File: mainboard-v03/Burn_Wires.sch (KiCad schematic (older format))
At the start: 41 parts, among them Q2 2N5088, Q3 2N5088, Q4 IRLML2803, Q5 IRLML2803, Q6 IRLML2803, Q7 IRLML2803, Q8 IRLML2803, U16 PE014006, U17 PE014006, U18 NDS8434, U19 NDS8434, U20 NDS8434, U21 NDS8434, U22 NDS8434

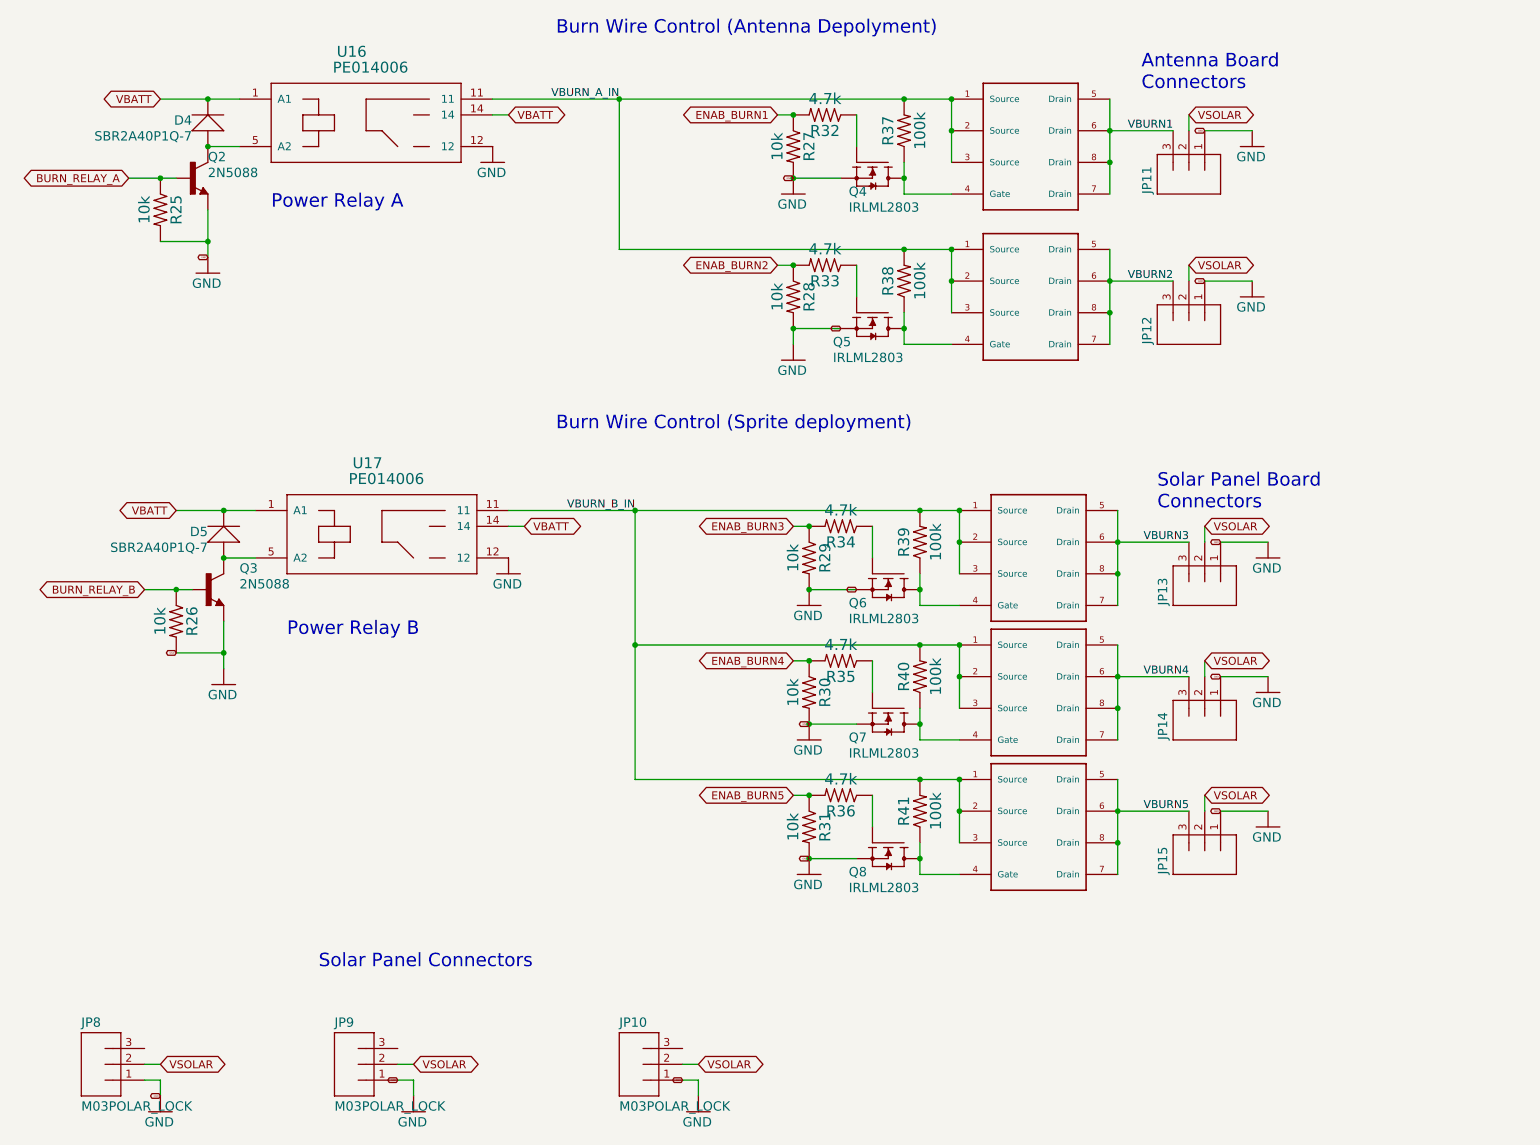
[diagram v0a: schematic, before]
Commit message: cleaning up schematic scheets
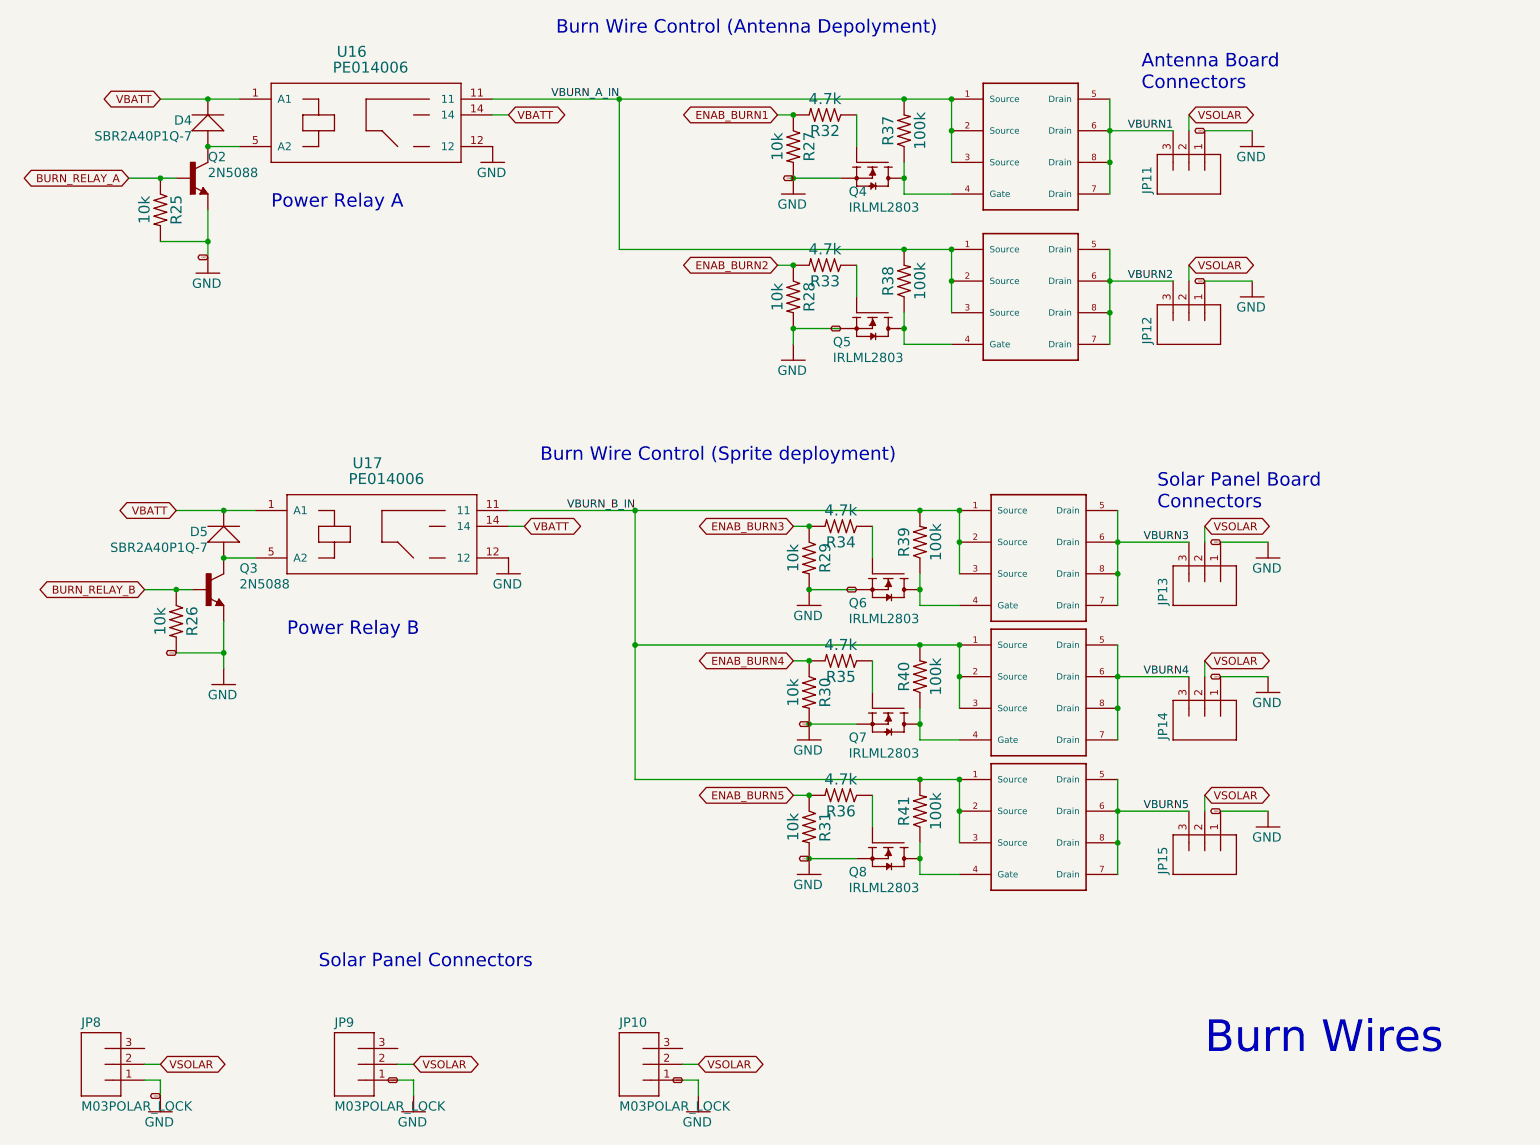
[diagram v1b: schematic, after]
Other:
- note added: "Burn Wires"
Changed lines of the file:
@@
 $Descr User 11693 8548
 encoding utf-8
-Sheet 6 6
+Sheet 2 6
 Title "PyCubed Mainboard"
 Date ""
-Rev "v02"
+Rev "v03"
 Comp "Stanford University"
 Comment1 "rexlab.stanford.edu"
@@
 Text Notes 4500 800  0    85   ~ 0
 Burn Wire Control (Antenna Depolyment)
-Text Notes 4500 3300 0    85   ~ 0
+Text Notes 4400 3500 0    85   ~ 0
 Burn Wire Control (Sprite deployment)
 Text Notes 2800 4600 0    85   ~ 0
@@
 Wire Wire Line
 	5000 3800 5000 4650
+Text Notes 8600 7250 0    200  ~ 0
+Burn Wires
 $EndSCHEMATC

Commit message: mainboardv3 clean up
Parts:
- removed D5: SBR2A40P1Q-7, kmb-test:PWRDI-123, symbol mainboard:DFLS130L
- removed Q3: 2N5088, kmb-test:SOT23, symbol mainboard:BC846
- removed Q6, Q7, Q8: IRLML2803, kmb-test:SOT-23, symbol mainboard:IRLML2803TRPBF
- removed R26, R29, R30, R31: 10k, Resistor_SMD:R_0603_1608Metric, symbol mainboard:RESISTOR0603
- removed R34, R35, R36: 4.7k, Resistor_SMD:R_0603_1608Metric, symbol mainboard:RESISTOR0603
- removed R39, R40, R41: 100k, Resistor_SMD:R_0603_1608Metric, symbol mainboard:RESISTOR0603
- removed U17: PE014006, kmb-test:RELAY5-PE_CO, symbol mainboard:PE014005
- removed U20, U21, U22: NDS8434, custom-footprints:NDS8434, symbol symbols:NDS8434
- D4: value SBR2A40P1Q-7 -> MBR120LSF; footprint kmb-test:PWRDI-123 -> mainboard:PWRDI-123
- JP10, JP11, JP12, JP13, JP14, JP15, JP8, JP9: footprint kmb-test:MOLEX-1X3_LOCK -> mainboard:MOLEX-1X3_LOCK
- Q2: footprint kmb-test:SOT23 -> mainboard:SOT23; Flight (none) -> 2N5088; Proto (none) -> S8050
- Q4: footprint kmb-test:SOT-23 -> mainboard:SOT-23; Flight (none) -> IRLML2803; Proto (none) -> 2302
- Q5: footprint kmb-test:SOT-23 -> mainboard:SOT-23
- U16: footprint kmb-test:RELAY5-PE_CO -> mainboard:RELAY5-PE_CO; Flight (none) -> PE014006 TE; Proto (none) -> JE-109D GOODSKY
- U18: Field4 ON Semiconductor -> (none); Field5 Unavailable -> (none); Field6 None -> (none); Field7 NDS8434 -> (none); Field8 SO-8 ON Semiconductor -> (none); Flight (none) -> NDS8434; Proto (none) -> DMP2022LSS-13
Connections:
- net VBURN3: no longer names the net of JP13.3
- net VBURN4: no longer names the net of JP14.3
- net VBURN5: no longer names the net of JP15.3
- no-connect marks 0 -> 6
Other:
- note removed: "Burn Wire Control (Sprite deployment)"
- note removed: "Power Relay B"
- note removed: "Solar Panel Board\nConnectors"
